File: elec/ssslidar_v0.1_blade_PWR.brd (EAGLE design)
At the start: 12.5 x 5 mm, 22 parts, among them P1 PIN_SMD_0.8X1_RECT, P10 PIN_SMD_0.8X1_RECT, P11 PIN_SMD_1X1_RECT, P12 PIN_SMD_0.8X1_RECT, P13 PIN_SMD_0.8X1_RECT, P16 PIN_SMD_0.8X1_RECT, P17 PIN_SMD_1X1_RECT, P18 PIN_SMD_0.8X1_RECT, P2 PIN_SMD_1X1_RECT, P3 PIN_SMD_0.8X1_RECT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

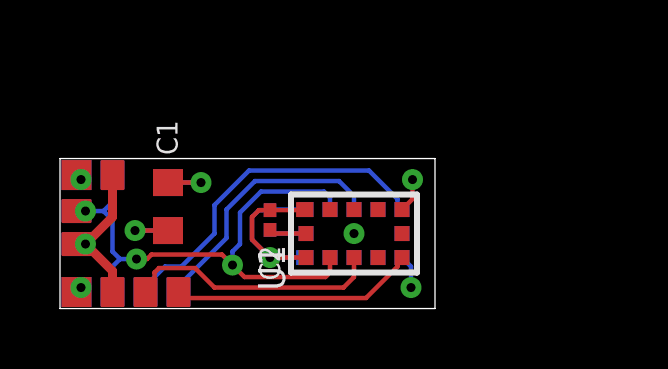
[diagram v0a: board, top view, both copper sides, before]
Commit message: Working on main board Made blades longer to avoid too much occlusion from the main PCB (but we will still need to put the whole thing on a mast).
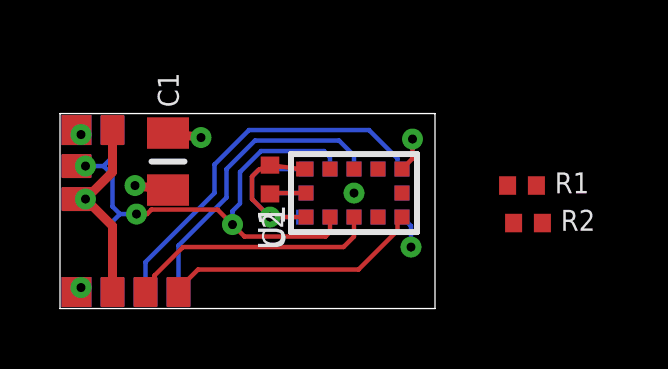
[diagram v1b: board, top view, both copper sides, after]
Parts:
- removed C3: 4.7uF, Xevelabs:0603_N
- removed C4: 100nF, Xevelabs:0201_N
- added R1, R2: (no value), Xevelabs:0402_N
- C1: value 4.7uF -> 10uF; device Xevelabs:0603_N -> Xevelabs:0805_N
- C2: device Xevelabs:0201_N -> Xevelabs:0402_N
- moved C1 1.50 mm to (3.60, 4.90)
- moved P1 1.50 mm to (1.75, 5.95)
- moved P10 1.50 mm to (0.55, 4.75)
- moved P12 1.50 mm to (0.55, 4.75)
- moved P13 1.50 mm to (0.55, 3.65)
- moved P16 1.50 mm to (0.55, 3.65)
- moved P18 1.50 mm to (1.75, 5.95)
- moved P2 1.50 mm to (0.55, 5.95)
- moved P9 1.50 mm to (0.55, 5.95)
- moved U1 1.35 mm to (9.80, 3.85)
- moved U2 1.35 mm to (9.80, 3.85)
- moved C2 1.35 mm to (7.00, 4.30)
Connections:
- net GND: no longer C3.2, C4.2
- net SDA1: now also R2.1
- net SDA2: now also R1.1
- net VDD: now also R1.2, R2.2; no longer C3.1, C4.1
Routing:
- net SCL: track 19.1 -> 20.7 mm
- net SDA2: track 8.71 -> 10.3 mm
- net GND: track 5.55 -> 4.24 mm
- net INT2: track 11.6 -> 12.8 mm
- net INT1: track 8.18 -> 9.00 mm
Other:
- board size 12.5 x 5 mm -> 12.5 x 6.5 mm

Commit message: Updated blades (ready for release). Double power rail for sensors.
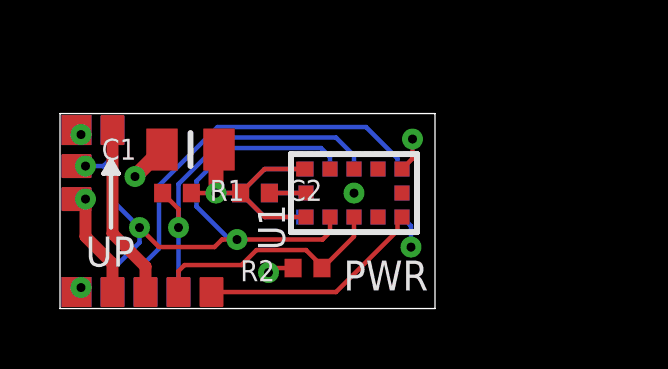
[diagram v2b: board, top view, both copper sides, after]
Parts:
- added C3: 100nF, Xevelabs:0402_N
- added P14: PIN_SMD_0.8X1_RECT, Xevelabs:PIN_SMD_0.8X1_RECT
- R1, R2: value (none) -> 2k
- moved R1 11.5 mm to (3.90, 3.85)
- moved R2 7.50 mm to (8.25, 1.35), turned to 180 degrees
- moved P4 1.10 mm to (3.95, 0.55)
- moved P6 1.10 mm to (5.05, 0.55)
- moved C1 0.85 mm to (4.35, 5.30), turned to 180 degrees
- moved C2 0.67 mm to (6.50, 3.85), turned to 0 degrees
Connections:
- new net VDD_PASS: P1.PIN, P14.PIN
- net GND: now also C3.2
- net VDD: now also C3.1; no longer P1.PIN
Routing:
- net VDD_PASS: track 0.00 -> 5.86 mm
- net VDD: track 19.1 -> 21.5 mm
- net SCL: track 20.7 -> 23.0 mm
- net SDA2: track 10.3 -> 12.4 mm, vias 0 -> 1
- net INT1: track 9.00 -> 7.56 mm
- net INT2: track 12.8 -> 13.5 mm
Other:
- board text added: "PWR"
- board text added: "UP"

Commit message: Made blades slightly taller (7mm instead of 6.5)
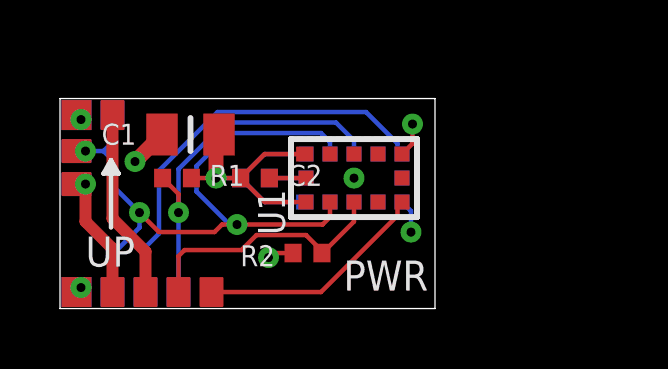
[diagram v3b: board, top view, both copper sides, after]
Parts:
- moved P13 0.50 mm to (0.55, 4.15)
- moved P16 0.50 mm to (0.55, 4.15)
- moved C1 0.50 mm to (4.35, 5.80)
- moved P1 0.50 mm to (1.75, 6.45)
- moved P10 0.50 mm to (0.55, 5.25)
- moved P12 0.50 mm to (0.55, 5.25)
- moved P18 0.50 mm to (1.75, 6.45)
- moved P2 0.50 mm to (0.55, 6.45)
- moved P9 0.50 mm to (0.55, 6.45)
- moved R2 0.50 mm to (8.25, 1.85)
- moved C2 0.50 mm to (6.50, 4.35)
- moved C3 0.50 mm to (6.50, 4.35)
- moved R1 0.50 mm to (3.90, 4.35)
- moved U1 0.50 mm to (9.80, 4.35)
- moved U2 0.50 mm to (9.80, 4.35)
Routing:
- net VDD_PASS: track 5.86 -> 6.36 mm
- net VDD: track 21.5 -> 22.0 mm
- net SDA1: track 8.21 -> 8.71 mm
- net SCL: track 23.0 -> 23.5 mm
- net INT2: track 13.5 -> 14.0 mm
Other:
- board size 12.5 x 6.5 mm -> 12.5 x 7 mm

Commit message: Routing done.
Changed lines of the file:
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@@
 <layer number="97" name="Info" color="7" fill="1" visible="no" active="no"/>
 <layer number="98" name="Guide" color="6" fill="1" visible="no" active="no"/>
+<layer number="99" name="SpiceOrder" color="5" fill="1" visible="no" active="no"/>
 <layer number="100" name="Muster" color="7" fill="1" visible="no" active="no"/>
 <layer number="101" name="Patch_Top" color="12" fill="4" visible="no" active="yes"/>
@@
 <text x="2.4" y="1.4" size="1" layer="22" font="vector" ratio="15" rot="MR0">UP</text>
 <text x="0.85" y="1.4" size="1" layer="21" font="vector" ratio="15">UP</text>
-<wire x1="1.7" y1="4.75" x2="1.7" y2="4.55" width="0.15" layer="22"/>
-<wire x1="1.7" y1="4.55" x2="1.7" y2="2.7" width="0.15" layer="22"/>
+<wire x1="1.7" y1="4.75" x2="1.7" y2="2.7" width="0.15" layer="22"/>
 <wire x1="1.95" y1="4.5" x2="1.7" y2="4.95" width="0.15" layer="21"/>
 <wire x1="1.7" y1="4.95" x2="1.45" y2="4.5" width="0.15" layer="21"/>
@@
 <wire x1="1.7" y1="4.55" x2="1.7" y2="2.7" width="0.15" layer="21"/>
 <text x="9.45" y="0.6" size="1" layer="21" font="vector" ratio="15">PWR</text>
+<circle x="8.15" y="6.15" radius="0.25" width="0" layer="21"/>
+<circle x="8.2" y="2.6" radius="0.25" width="0" layer="22"/>
 </plain>
 <attributes>
